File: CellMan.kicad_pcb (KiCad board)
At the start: 2 copper layers, 100 x 45 mm, 74 parts, among them J1 Conn_01x04_Male, J2 Conn_01x04_Male, J3 Conn_01x04_Male, J4 Conn_01x02_Female, J5 Conn_01x03_Male, Q1 BSS138W, Q2 STS8DN6LF6AG, Q4 BSS138W, Q5 BSS138W, SW1 SW_DIP_x06, SW2 SW_DIP_x04, U1 MCP23008, U2 MCP9808, U3 ADC128D818, U4 ACHS-7121, U5 MCP6004, U8 OPA347, U9 OPA347

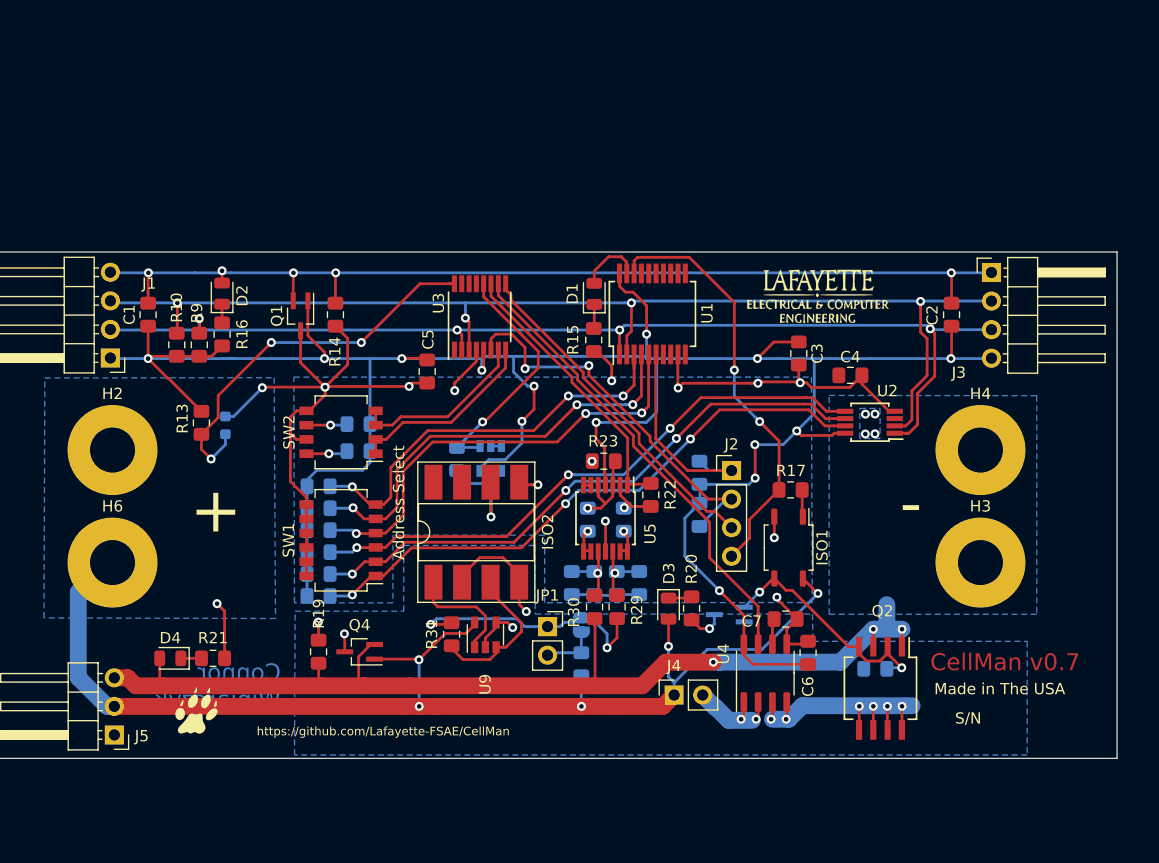
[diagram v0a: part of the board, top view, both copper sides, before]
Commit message: Started work on post-design review version
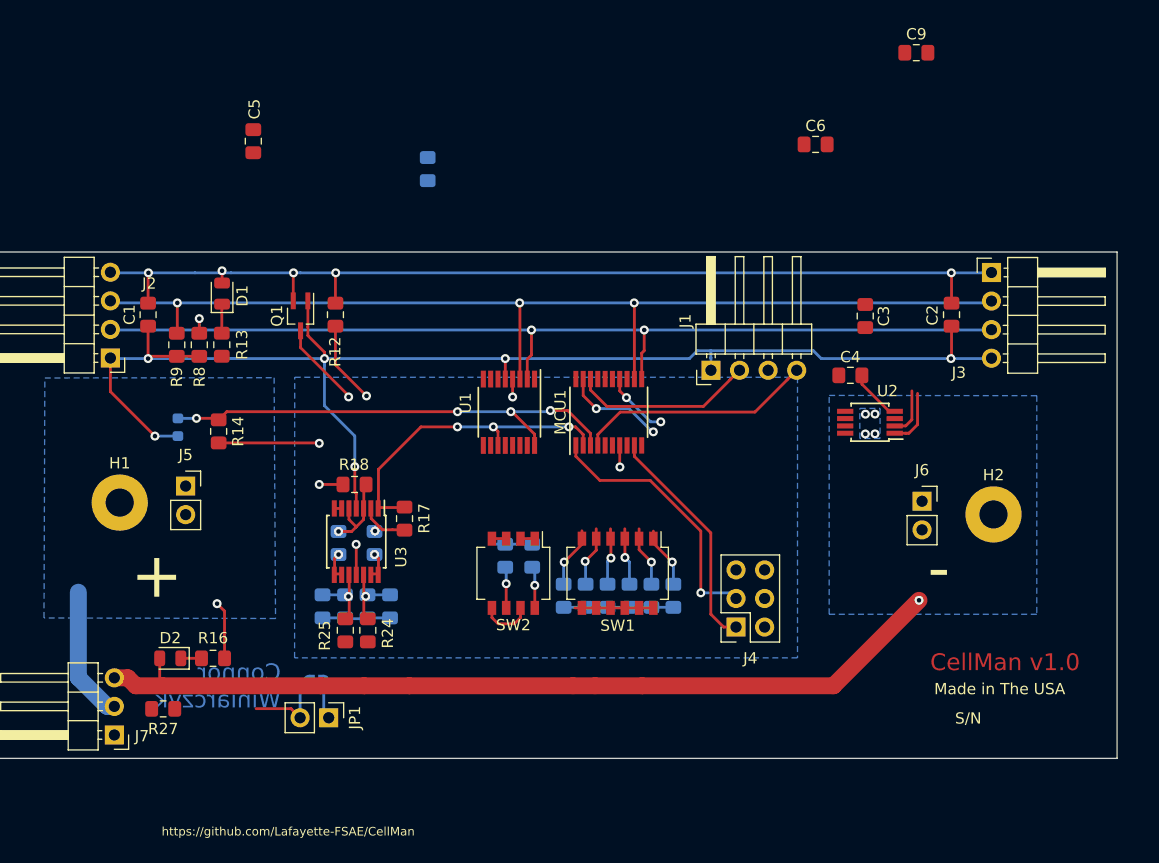
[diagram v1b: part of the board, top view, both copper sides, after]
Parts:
- removed the C7 at (162.2, 115.0)
- removed the D1 at (145.2, 86.1)
- removed D3: LED, LED_SMD:LED_0805_2012Metric
- removed G***: LOGO, Lafayette_Electric_Car_Footprints:Paw
- removed G***: LOGO, Lafayette_Electric_Car_Footprints:ECE_Logo
- removed H3, H4, H6: MountingHole_Pad, MountingHole:MountingHole_4mm_Pad
- removed ISO1: VOM617A, Package_SO:SOP-4_3.8x4.1mm_P2.54mm
- removed ISO2: HCNR200, Package_DIP:DIP-8_W8.89mm_SMDSocket_LongPads
- removed the J2 at (157.4, 101.8)
- removed Q2: STS8DN6LF6AG, Package_SO:SO-8_5.3x6.2mm_P1.27mm
- removed Q4, Q5: BSS138W, Package_TO_SOT_SMD:SOT-323_SC-70_Handsoldering
- removed R15, R26, R31: R, Resistor_SMD:R_0805_2012Metric_Pad1.15x1.40mm_HandSolder
- removed the R17 at (162.7, 103.5)
- removed the R18 at (170.2, 119.4)
- removed the R19 at (120.7, 117.9)
- removed the R20 at (153.8, 114.0)
- removed the R7 at (154.6, 102.0)
- removed the U1 at (150.4, 87.9)
- removed U4: ACHS-7121, Package_SO:SO-8_3.9x4.9mm_P1.27mm
- removed U8, U9: OPA347, Package_TO_SOT_SMD:SOT-23-5
- added C9: 1uF, Capacitor_SMD:C_0805_2012Metric_Pad1.15x1.40mm_HandSolder, F.Cu at (173.8, 64.7)
- added H1: MountingHole_Pad, MountingHole:MountingHole_2.5mm_Pad, F.Cu at (103.0, 104.7)
- added J1: Conn_01x04_Female, Connector_PinHeader_2.54mm:PinHeader_1x04_P2.54mm_Horizontal, F.Cu at (155.6, 92.9)
- added J5: Conn_01x02_Female, Connector_PinSocket_2.54mm:PinSocket_1x02_P2.54mm_Vertical, F.Cu at (108.9, 103.2)
- added J6: Conn_01x02_Female, Connector_PinSocket_2.54mm:PinSocket_1x02_P2.54mm_Vertical, F.Cu at (174.3, 104.5)
- added MCU1: STM8S003F3, Package_SO:TSSOP-20_4.4x6.5mm_P0.65mm, F.Cu at (146.5, 96.6)
- H2: footprint MountingHole:MountingHole_4mm_Pad -> MountingHole:MountingHole_2.5mm_Pad
- J4: value Conn_01x02_Female -> Conn_01x06_Female; footprint Connector_PinSocket_2.54mm:PinSocket_1x02_P2.54mm_Vertical -> Connector_PinSocket_2.54mm:PinSocket_2x03_P2.54mm_Vertical
- JP1: footprint Connector_PinSocket_2.54mm:PinSocket_1x02_P2.54mm_Vertical -> Connector_PinHeader_2.54mm:PinHeader_1x02_P2.54mm_Vertical
- R1, R2, R3, R4, R5, R6: value 5k -> 20k
- R10: renamed from R11; value 5k -> 20k
- R11: renamed from R12; value 5k -> 20k
- R27: renamed from R32; moved to F.Cu
- R7: renamed from R8; value 5k -> 20k
- moved H2 78.5 mm to (180.7, 105.7)
- moved C6 45.2 mm to (164.9, 72.8), turned to 0 degrees
- moved R7 39.1 mm to (130.4, 75.0)
- moved R27 37.4 mm to (106.9, 123.0), turned to 0 degrees
- moved R1 31.5 mm to (152.2, 112.9), turned to 90 degrees
- moved R2 29.6 mm to (150.3, 112.9), turned to 90 degrees
- moved R3 27.9 mm to (148.3, 112.9), turned to 90 degrees
- moved R4 26.3 mm to (146.4, 112.9), turned to 90 degrees
- moved C5 25.6 mm to (114.9, 72.5)
- moved R5 25.0 mm to (144.4, 112.9), turned to 90 degrees
- moved SW1 24.8 mm to (147.3, 110.9), turned to 270 degrees
- moved JP2 24.1 mm to (120.5, 120.7), turned to 180 degrees
- moved R6 23.9 mm to (142.5, 112.9), turned to 90 degrees
- moved R19 22.2 mm to (125.7, 108.2)
- moved R18 22.2 mm to (123.9, 103.0)
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- renumbered C8 to C7, C9 to C8, D2 to D1, D4 to D2, J1 to J2, J5 to J7, R14 to R12, R16 to R13, R13 to R14, R21 to R16, R22 to R17, R23 to R18, R24 to R19, R25 to R20, R27 to R22, R28 to R23, R29 to R24, R30 to R25, R9 to R8, R10 to R9, U3 to U1, U5 to U3
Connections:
- net /CellVoltage_02 renamed /CellVoltage
- C1 pad 1: +5V -> +3V3
- C2 pad 1: +5V -> +3V3
- C3 pad 1: +5V -> +3V3
- C4 pad 1: +5V -> +3V3
- C5 pad 1: +5V -> +3V3
- C6 pad 1: +5V -> /SafeGND
- C6 pad 2: /SafeGND -> /Ref_Cap
- H2 pad 1: /Cell+ -> /Cell-
- J2 pad 1: +5V -> +3V3
- J3 pad 4: +5V -> +3V3
- J4 pad 1: /Cell+ -> +3V3
- J4 pad 2: Net-(J4-Pad2) -> /SafeGND
- J7 pad 1: Net-(J5-Pad1) -> (no net)
- Q1 pad 1: +5V -> +3V3
- R1 pad 1: +5V -> /Address_T0
- R1 pad 2: /Address_T0 -> +3V3
- R10 pad 1: +5V -> +3V3
- R11 pad 1: +5V -> +3V3
- R13 pad 1: +5V -> +3V3
- R14 pad 1: /Temperature -> /SafeGND
- R14 pad 2: +5V -> /Temperature
- R2 pad 1: +5V -> +3V3
- R3 pad 1: +5V -> +3V3
- R4 pad 1: +5V -> +3V3
- R5 pad 1: +5V -> +3V3
- R6 pad 1: +5V -> +3V3
- R7 pad 1: +5V -> Net-(R7-Pad1)
- R7 pad 2: /~ADC_INT -> +3V3
- R8 pad 1: +5V -> +3V3
- R9 pad 1: +5V -> +3V3
- TH1 pad 1: /Temperature -> +3V3
- TH1 pad 2: /SafeGND -> /Temperature
- U1 pad 1: Net-(U3-Pad1) -> (no net)
- U1 pad 10: /BalanceCurrent -> (no net)
- U1 pad 12: /CellVoltage_01 -> (no net)
- U1 pad 13: Net-(U3-Pad13) -> (no net)
- U1 pad 14: Net-(U3-Pad14) -> (no net)
- U1 pad 15: Net-(U3-Pad15) -> (no net)
- U1 pad 5: +5V -> +3V3
- U1 pad 6: /~ADC_INT -> Net-(R7-Pad1)
- U1 pad 9: /ADC_Sanity_Check -> (no net)
- U2 pad 3: Net-(U2-Pad3) -> (no net)
- U2 pad 8: +5V -> +3V3
- U3 pad 4: +5V -> +3V3
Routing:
- net +5V: track 230.0 -> 0.00 mm, vias 14 -> 0
- net +3V3: track 0.00 -> 160.4 mm, vias 0 -> 6
- net /Cell+: track 116.8 -> 17.5 mm, vias 6 -> 1
- net /SafeGND: track 108.5 -> 54.9 mm, vias 13 -> 7
- net /Address_T0: track 53.6 -> 5.81 mm, vias 3 -> 1
- net /Address_T1: track 52.6 -> 5.38 mm, vias 3 -> 1
- net /Address_T2: track 52.1 -> 5.10 mm, vias 3 -> 1
- net /BalanceCurrent: track 41.6 -> 5.84 mm, vias 0 -> 2
- net /Address_G0: track 39.9 -> 5.06 mm, vias 3 -> 1
- net /~ADC_INT: track 34.7 -> 0.00 mm, vias 2 -> 0
- net /Address_G1: track 38.4 -> 5.44 mm, vias 3 -> 1
- net /Address_G2: track 37.5 -> 5.42 mm, vias 3 -> 1
- net /ADC_Sanity_Check: track 30.4 -> 0.00 mm
- net Net-(Q2-Pad5): track 24.2 -> 0.00 mm, vias 6 -> 0
- net /Balancing: track 21.8 -> 0.00 mm, vias 2 -> 0
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- removed copper zone on B.Cu, net /SafeCell-
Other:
- board text added: "CellMan v1.0"
- board text removed: "Address Select"
- board text removed: "CellMan v0.7"

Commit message: Zero unrouted traces baby! Wait, where have I heard that before?
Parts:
- added D3: LED, LED_SMD:LED_0805_2012Metric, F.Cu at (142.8, 90.4)
- added R15: R, Resistor_SMD:R_0805_2012Metric_Pad1.15x1.40mm_HandSolder, F.Cu at (144.8, 90.4)
- R7: moved to F.Cu
- moved C9 39.9 mm to (155.4, 100.0), turned to 90 degrees
- moved C3 36.2 mm to (133.2, 90.5)
- moved C6 29.5 mm to (153.4, 100.0), turned to 90 degrees
- moved C5 28.7 mm to (125.3, 99.3), turned to 90 degrees
- moved R7 16.2 mm to (135.3, 90.5), turned to 90 degrees
- moved R27 7.10 mm to (114.0, 123.0)
- moved J4 6.34 mm to (162.0, 111.0), turned to 90 degrees
- moved D2 4.21 mm to (111.6, 117.6), turned to 0 degrees
- moved R16 3.61 mm to (107.8, 117.6), turned to 0 degrees
- moved R10 2.03 mm to (137.8, 110.1)
- moved R2 2.03 mm to (148.4, 113.7)
- moved R3 2.03 mm to (146.4, 113.7)
- moved R5 2.03 mm to (142.5, 113.7)
- moved SW1 2.03 mm to (145.4, 111.7)
- moved R1 2.03 mm to (150.3, 113.7), turned to 270 degrees
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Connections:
- J4 pad 1: +3V3 -> /BalanceCurrent
- J4 pad 2: /SafeGND -> /Feedback
- J4 pad 4: /Feedback -> /Extra
- J4 pad 5: /BalanceCurrent -> +3V3
- J4 pad 6: (no net) -> /SafeGND
- MCU1 pad 17: (no net) -> /Indicator
- MCU1 pad 20: (no net) -> /Extra
- U1 pad 7: /Address_A1 -> /Address_A0
- U1 pad 8: /Address_A0 -> /Address_A1
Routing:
- net +3V3: track 160.4 -> 219.8 mm, vias 6 -> 10
- net /SafeGND: track 54.9 -> 92.6 mm, vias 7 -> 16
- net /Extra: track 0.00 -> 34.1 mm, vias 0 -> 2
- net /Address_T2: track 5.10 -> 31.8 mm, vias 1 -> 2
- net /Address_T1: track 5.38 -> 29.2 mm, vias 1 -> 2
- net /Cell+: track 17.5 -> 40.2 mm
- net /Address_T0: track 5.81 -> 28.2 mm, vias 1 -> 2
- net /BalanceCurrent: track 5.84 -> 27.8 mm
- net /Feedback: track 9.04 -> 29.4 mm
- net /Address_A0: track 1.27 -> 17.8 mm
- net /Address_A1: track 1.27 -> 17.5 mm
- net /Cell-: track 78.7 -> 94.4 mm, vias 1 -> 5
- net Net-(JP1-Pad1): track 3.25 -> 13.4 mm, vias 0 -> 1
- net /SCL: track 99.0 -> 107.2 mm, vias 3 -> 4
- net /Ref_Cap: track 0.00 -> 7.67 mm
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- added copper zone on F.Cu, net /Cell-

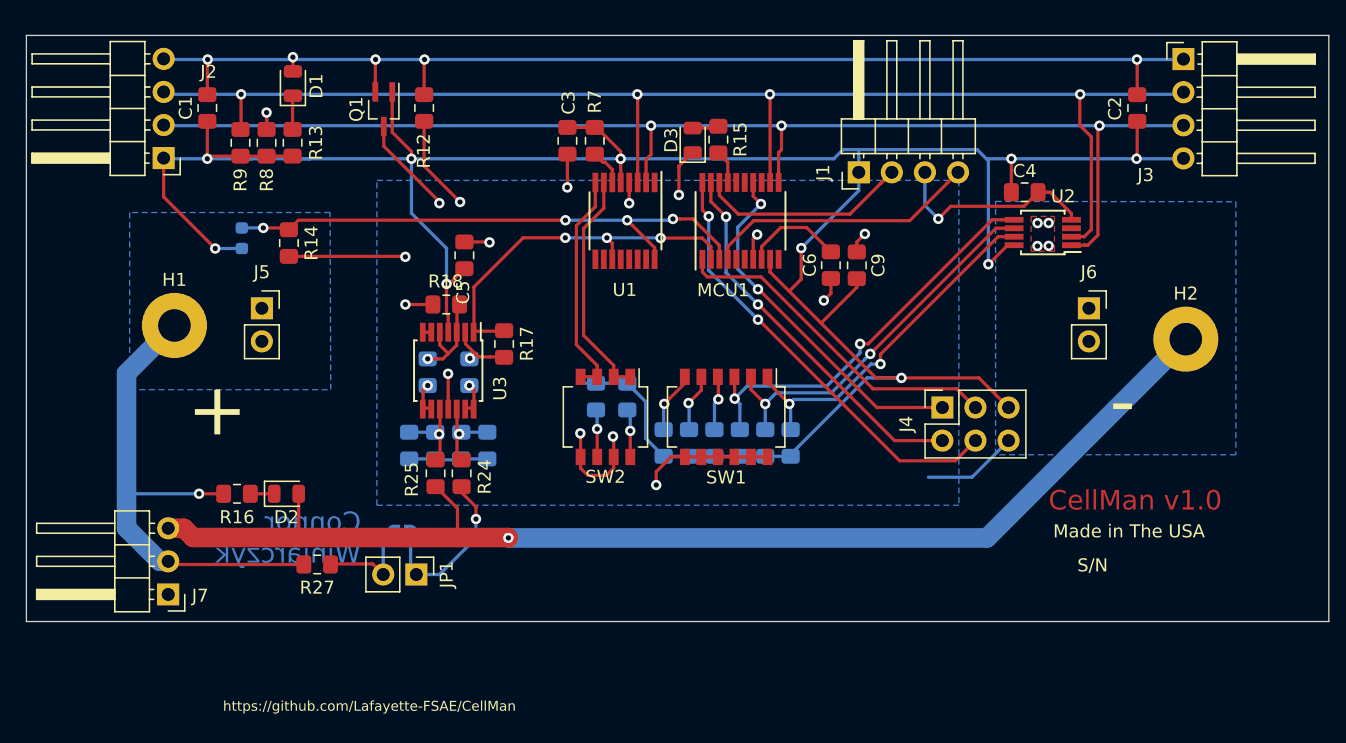
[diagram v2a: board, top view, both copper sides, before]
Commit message: adjusted mounting and added flair
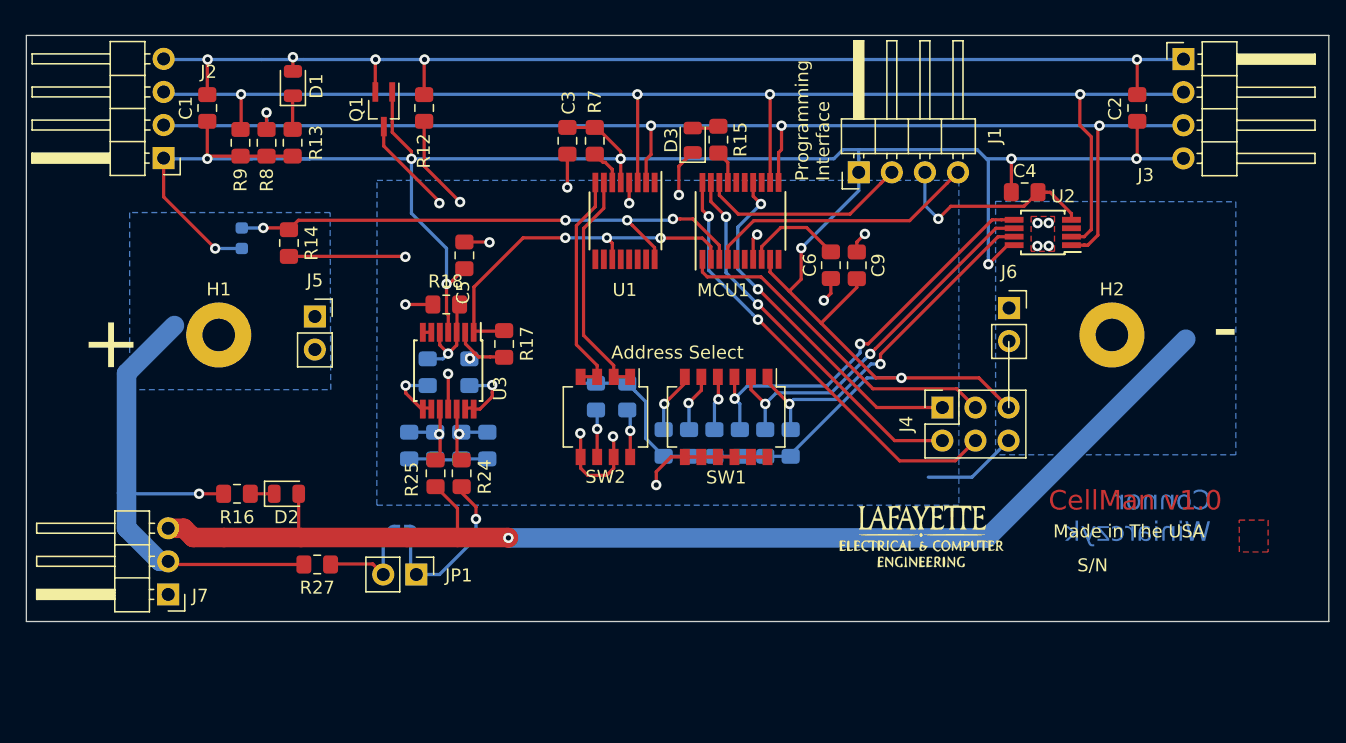
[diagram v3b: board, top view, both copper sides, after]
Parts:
- added G***: LOGO, Lafayette_Electric_Car_Footprints:paw_solder_mask, F.Cu at (185.9, 120.8)
- added G***: LOGO, Lafayette_Electric_Car_Footprints:ECE_Logo, F.Cu at (160.4, 120.9)
- moved J6 6.13 mm to (167.1, 103.3)
- moved H2 5.68 mm to (175.0, 105.4)
- moved J5 4.12 mm to (113.8, 104.0)
- moved H1 3.48 mm to (106.4, 105.4)
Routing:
- net Net-(R19-Pad1): track 2.52 -> 5.13 mm
- net Net-(R20-Pad1): track 2.52 -> 4.75 mm
- added copper zone on F.Cu, net (none)
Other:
- board text added: "Address Select"
- board text added: "Designed by:"
- board text added: "Programming Interface"

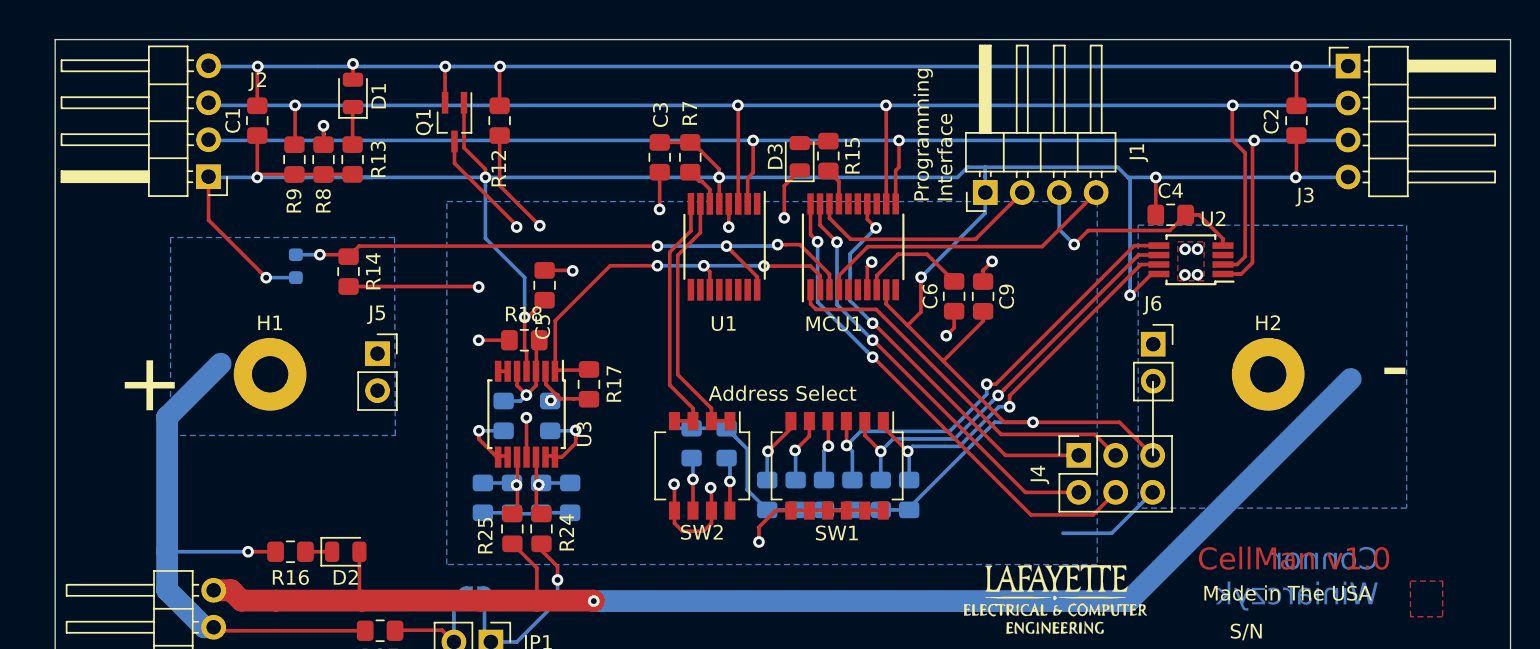
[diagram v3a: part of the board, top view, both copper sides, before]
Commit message: switched power supply to 24V (Seg+) and removed ADC
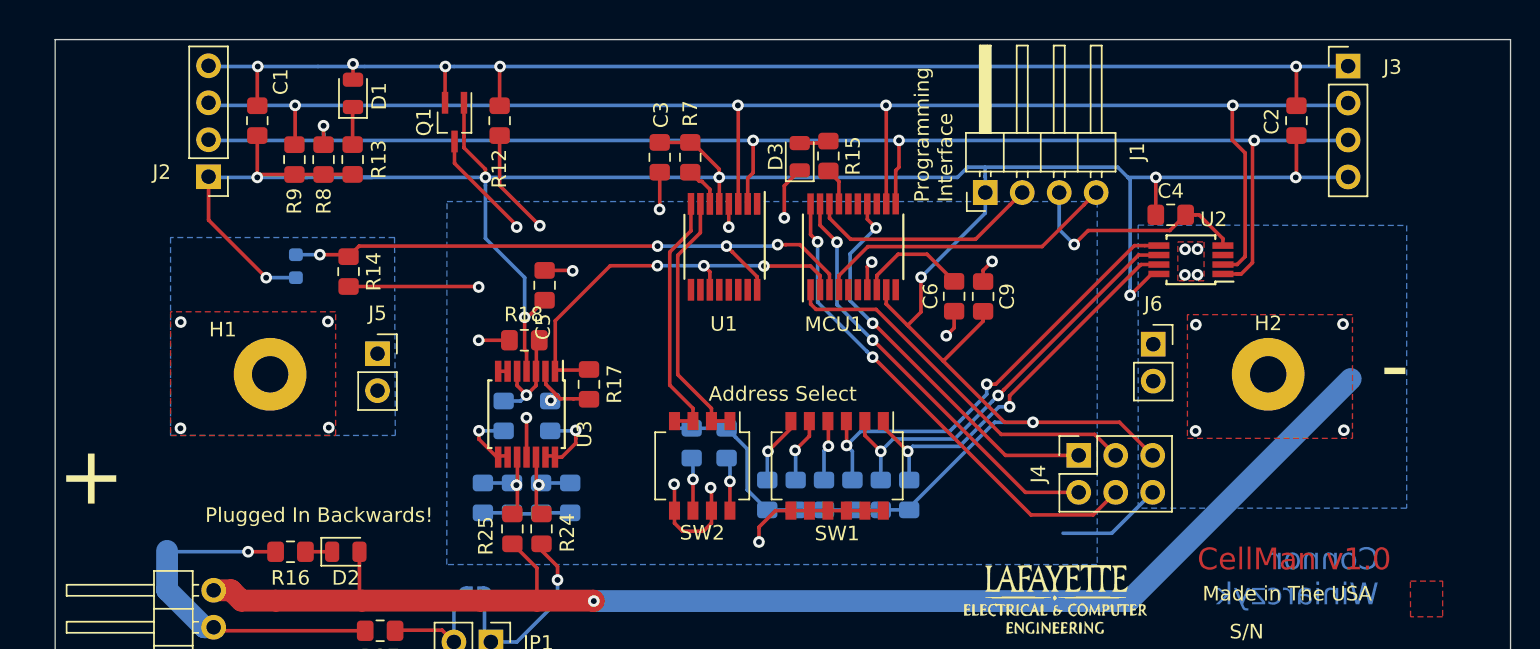
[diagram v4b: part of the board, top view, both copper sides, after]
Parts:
- J2, J3: footprint Connector_PinHeader_2.54mm:PinHeader_1x04_P2.54mm_Horizontal -> Connector_PinHeader_2.54mm:PinHeader_1x04_P2.54mm_Vertical
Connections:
- J7 pad 1: (no net) -> Net-(J7-Pad1)
- MCU1 pad 10: (no net) -> Net-(MCU1-Pad10)
- MCU1 pad 13: (no net) -> Net-(MCU1-Pad13)
- MCU1 pad 15: (no net) -> Net-(MCU1-Pad15)
- MCU1 pad 16: (no net) -> Net-(MCU1-Pad16)
- MCU1 pad 5: (no net) -> Net-(MCU1-Pad5)
- MCU1 pad 6: (no net) -> Net-(MCU1-Pad6)
- U1 pad 1: (no net) -> Net-(U1-Pad1)
- U1 pad 10: (no net) -> Net-(U1-Pad10)
- U1 pad 12: (no net) -> Net-(U1-Pad12)
- U1 pad 13: (no net) -> Net-(U1-Pad13)
- U1 pad 14: (no net) -> Net-(U1-Pad14)
- U1 pad 15: (no net) -> Net-(U1-Pad15)
- U1 pad 9: (no net) -> Net-(U1-Pad9)
- U2 pad 3: (no net) -> Net-(U2-Pad3)
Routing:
- net /Cell+: track 40.2 -> 25.8 mm, vias 1 -> 5
- net (no net): vias 0 -> 4
- added copper zone on F.Cu, net /Cell+
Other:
- board text added: "Plugged In Backwards!"
